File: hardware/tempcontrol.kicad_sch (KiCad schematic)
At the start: 11 parts, among them J10 FAN1, J12 FAN2, U15 EMC2305-x-AP

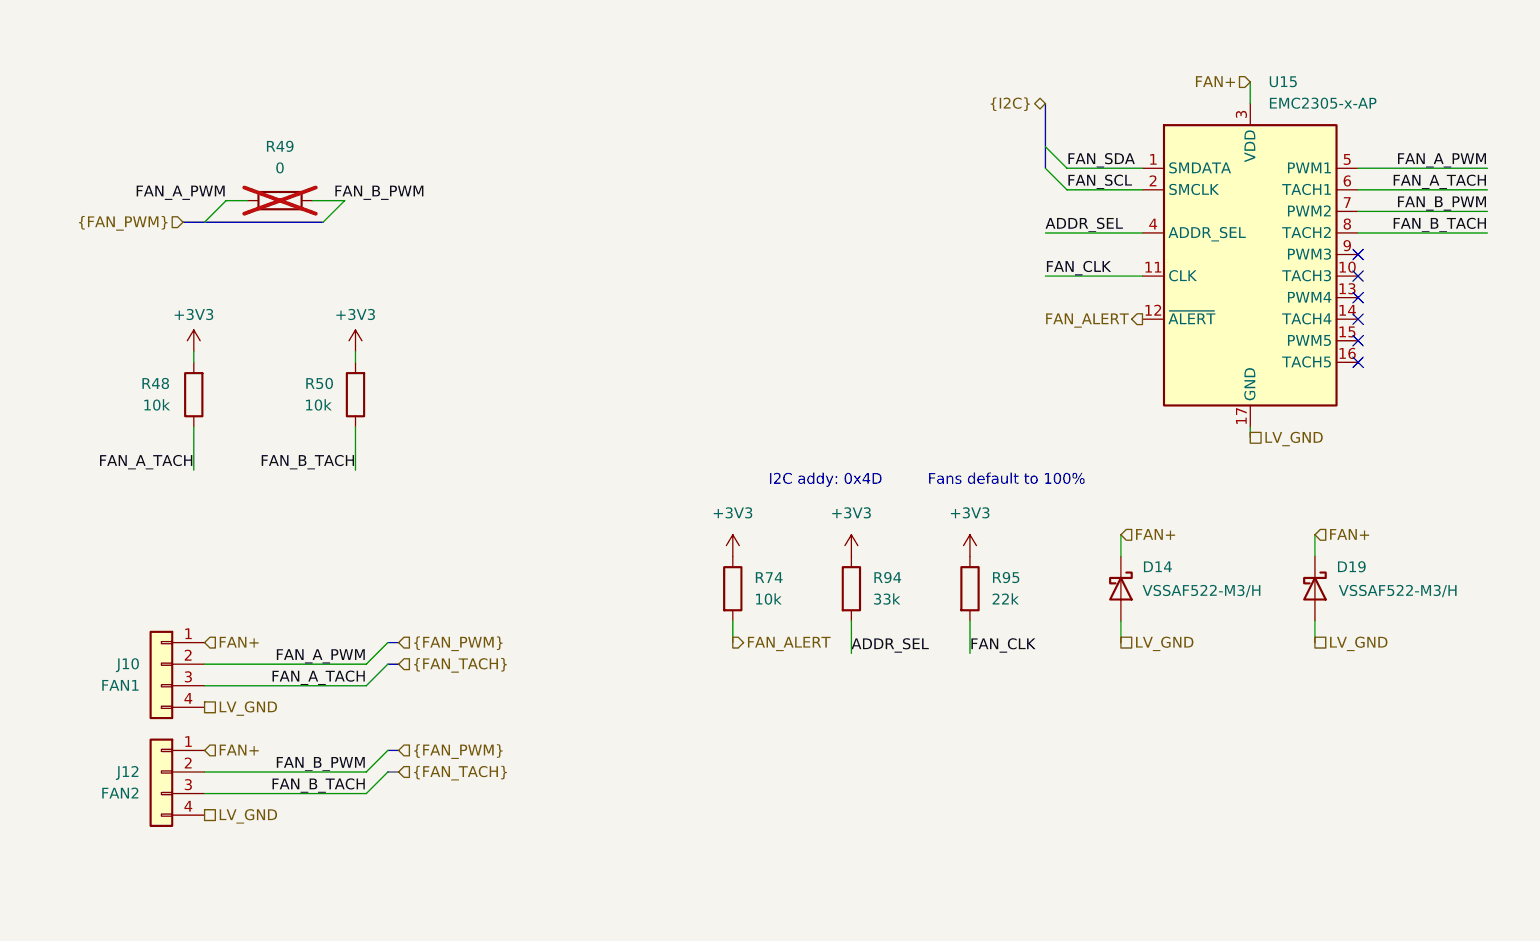
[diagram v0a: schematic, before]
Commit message: done all obbb specific reviews beside indicator led resistor values + math, goodnight
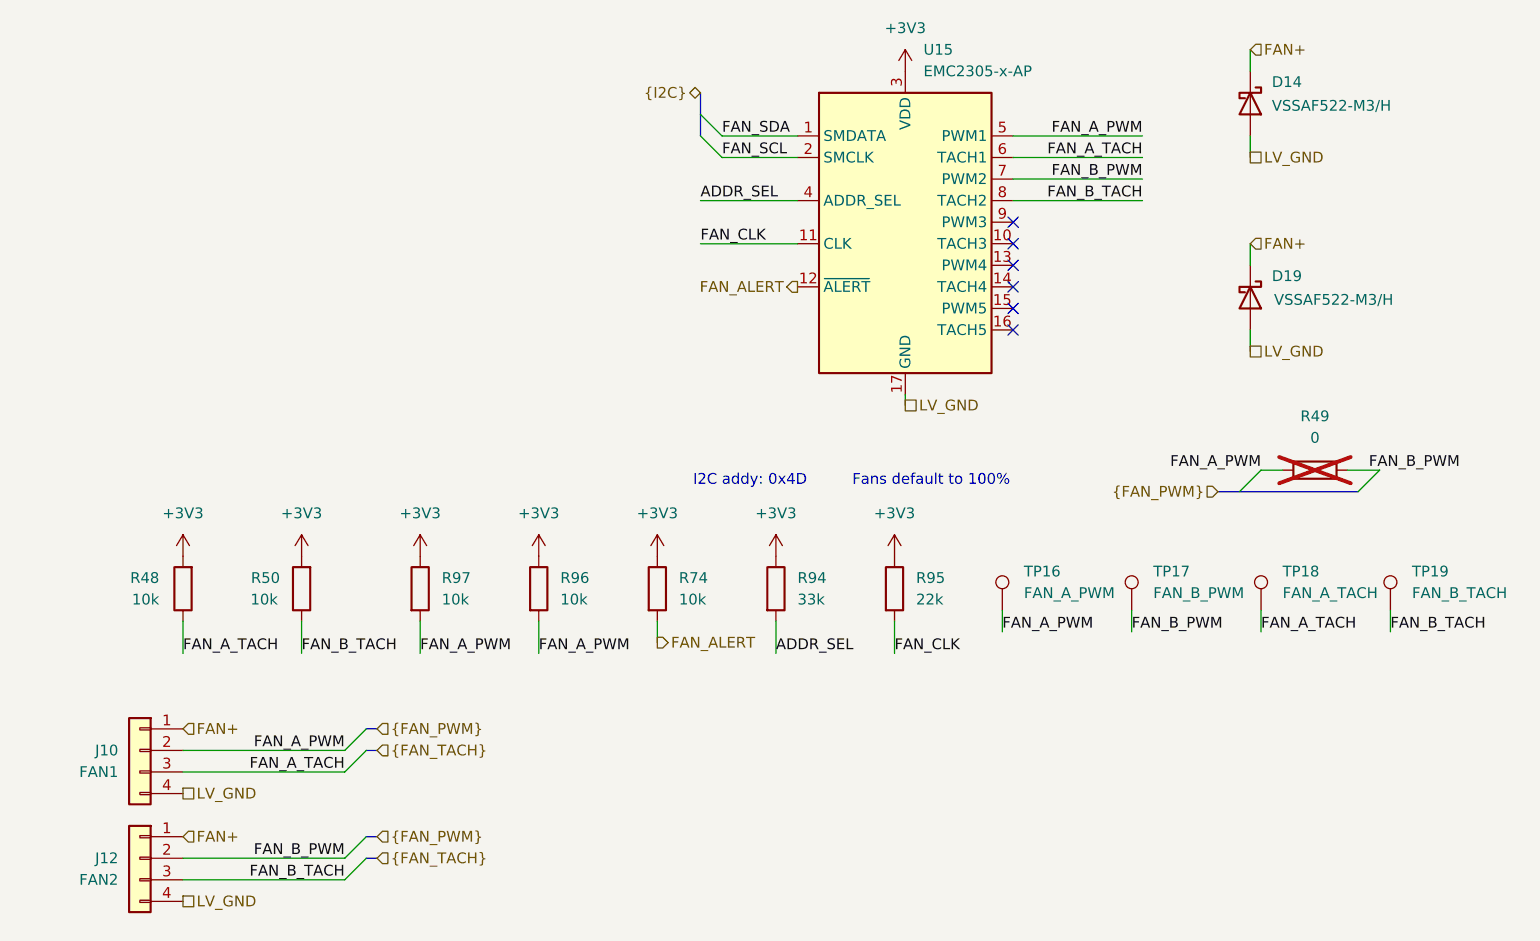
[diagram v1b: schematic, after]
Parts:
- added R96, R97: 10k, symbol Device:R
- added TP16: FAN_A_PWM, symbol Connector:TestPoint
- added TP17: FAN_B_PWM, symbol Connector:TestPoint
- added TP18: FAN_A_TACH, symbol Connector:TestPoint
- added TP19: FAN_B_TACH, symbol Connector:TestPoint
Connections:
- net +3V3: now also U15.3 (VDD), R96.1, R97.1
- net FAN+: no longer U15.3 (VDD)
- net FAN_A_PWM: now also R96.2, R97.2, TP16.1
- net FAN_A_TACH: now also TP18.1
- net FAN_B_PWM: now also TP17.1
- net FAN_B_TACH: now also TP19.1
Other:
- moved on the sheet: D14, D19, J10, J12, R48, R49, R50, R74, R94, R95, U15

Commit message: fixes only thing left is finish assigning footprints, its frozen
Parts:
- J10: renamed from J12; footprint (none) -> LHRS_Connectors:Molex_Nano-Fit_105309-xx04_1x04_P2.50mm_Vertical
- J9: renamed from J10; footprint (none) -> LHRS_Connectors:Molex_Nano-Fit_105309-xx04_1x04_P2.50mm_Vertical
- R88: renamed from R49; LCSC C21189 -> (none); LCSC P/N (none) -> C21189
- renumbered D14 to D20, D19 to D21, R48 to R81, R50 to R82, R97 to R83, R96 to R84, R74 to R85, R94 to R86, R95 to R87, TP16 to TP13, TP17 to TP14, TP18 to TP15, TP19 to TP16, U15 to U12
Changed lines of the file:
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@@
 		(dnp no)
 		(fields_autoplaced yes)
-		(property "Reference" "U15"
+		(property "Reference" "U12"
 			(at 126.6033 26.67 0)
 			(show_name no)
@@
 			(project "PS-LVCarrier"
 				(path "/9bab2d9d-20f3-40ef-8545-e1299efec47e/f9fba8b7-0cf3-4419-9ae4-4e9c55277e07"
-					(reference "U15")
+					(reference "U12")
 					(unit 1)
 				)
@@
 		(dnp no)
 		(fields_autoplaced yes)
-		(property "Reference" "R74"
+		(property "Reference" "R85"
 			(at 97.79 88.8999 0)
 			(show_name no)
@@
 			(project "PS-LVCarrier"
 				(path "/9bab2d9d-20f3-40ef-8545-e1299efec47e/f9fba8b7-0cf3-4419-9ae4-4e9c55277e07"
-					(reference "R74")
+					(reference "R85")
 					(unit 1)
 				)
@@
 		(in_pos_files yes)
 		(dnp no)
-		(property "Reference" "D19"
+		(property "Reference" "D21"
 			(at 167.64 53.34 90)
 			(show_name no)
@@
 			(project "PS-LVCarrier"
 				(path "/9bab2d9d-20f3-40ef-8545-e1299efec47e/f9fba8b7-0cf3-4419-9ae4-4e9c55277e07"
-					(reference "D19")
+					(reference "D21")
 					(unit 1)
 				)
@@
 		(dnp no)
 		(fields_autoplaced yes)
-		(property "Reference" "R96"
+		(property "Reference" "R84"
 			(at 83.82 88.8999 0)
 			(show_name no)
@@
 			(project "PS-LVCarrier"
 				(path "/9bab2d9d-20f3-40ef-8545-e1299efec47e/f9fba8b7-0cf3-4419-9ae4-4e9c55277e07"
-					(reference "R96")
+					(reference "R84")
 					(unit 1)
 				)
@@
 		(dnp no)
 		(fields_autoplaced yes)
-		(property "Reference" "TP19"
+		(property "Reference" "TP16"
 			(at 184.15 88.1379 0)
 			(show_name no)
@@
 			(project "PS-LVCarrier"
 				(path "/9bab2d9d-20f3-40ef-8545-e1299efec47e/f9fba8b7-0cf3-4419-9ae4-4e9c55277e07"
-					(reference "TP19")
+					(reference "TP16")
 					(unit 1)
 				)
@@
 		(dnp no)
 		(fields_autoplaced yes)
-		(property "Reference" "#PWR0172"
+		(property "Reference" "#PWR0104"
 			(at 124.46 33.02 0)
 			(hide yes)
@@
 			(project "PS-LVCarrier"
 				(path "/9bab2d9d-20f3-40ef-8545-e1299efec47e/f9fba8b7-0cf3-4419-9ae4-4e9c55277e07"
-					(reference "#PWR0172")
+					(reference "#PWR0104")
 					(unit 1)
 				)
@@
 		(dnp no)
 		(fields_autoplaced yes)
-		(property "Reference" "R97"
+		(property "Reference" "R83"
 			(at 69.85 88.8999 0)
 			(show_name no)
@@
 			(project "PS-LVCarrier"
 				(path "/9bab2d9d-20f3-40ef-8545-e1299efec47e/f9fba8b7-0cf3-4419-9ae4-4e9c55277e07"
-					(reference "R97")
+					(reference "R83")
 					(unit 1)
 				)
@@
 		(dnp no)
 		(fields_autoplaced yes)
-		(property "Reference" "#PWR0170"
+		(property "Reference" "#PWR097"
 			(at 39.37 90.17 0)
 			(hide yes)
@@
 			(project "PS-LVCarrier"
 				(path "/9bab2d9d-20f3-40ef-8545-e1299efec47e/f9fba8b7-0cf3-4419-9ae4-4e9c55277e07"
-					(reference "#PWR0170")
+					(reference "#PWR097")
 					(unit 1)
 				)
@@
 		(dnp no)
 		(fields_autoplaced yes)
-		(property "Reference" "TP18"
+		(property "Reference" "TP15"
 			(at 168.91 88.1379 0)
 			(show_name no)
@@
 			(project "PS-LVCarrier"
 				(path "/9bab2d9d-20f3-40ef-8545-e1299efec47e/f9fba8b7-0cf3-4419-9ae4-4e9c55277e07"
-					(reference "TP18")
+					(reference "TP15")
 					(unit 1)
 				)
@@
 		(in_pos_files yes)
 		(dnp no)
-		(property "Reference" "R50"
+		(property "Reference" "R82"
 			(at 50.8 88.9 0)
 			(show_name no)
@@
 			(project "PS-LVCarrier"
 				(path "/9bab2d9d-20f3-40ef-8545-e1299efec47e/f9fba8b7-0cf3-4419-9ae4-4e9c55277e07"
-					(reference "R50")
+					(reference "R82")
 					(unit 1)
 				)
@@
 		(dnp no)
 		(fields_autoplaced yes)
-		(property "Reference" "#PWR0168"
+		(property "Reference" "#PWR0100"
 			(at 81.28 90.17 0)
 			(hide yes)
@@
 			(project "PS-LVCarrier"
 				(path "/9bab2d9d-20f3-40ef-8545-e1299efec47e/f9fba8b7-0cf3-4419-9ae4-4e9c55277e07"
-					(reference "#PWR0168")
+					(reference "#PWR0100")
 					(unit 1)
 				)
@@
 		(dnp no)
 		(fields_autoplaced yes)
-		(property "Reference" "#PWR0165"
+		(property "Reference" "#PWR0101"
 			(at 95.25 90.17 0)
 			(hide yes)
@@
 			(project "PS-LVCarrier"
 				(path "/9bab2d9d-20f3-40ef-8545-e1299efec47e/f9fba8b7-0cf3-4419-9ae4-4e9c55277e07"
-					(reference "#PWR0165")
+					(reference "#PWR0101")
 					(unit 1)
 				)
@@
 		(dnp no)
 		(fields_autoplaced yes)
-		(property "Reference" "#PWR0169"
+		(property "Reference" "#PWR099"
 			(at 67.31 90.17 0)
 			(hide yes)
@@
 			(project "PS-LVCarrier"
 				(path "/9bab2d9d-20f3-40ef-8545-e1299efec47e/f9fba8b7-0cf3-4419-9ae4-4e9c55277e07"
-					(reference "#PWR0169")
+					(reference "#PWR099")
 					(unit 1)
 				)
@@
 		(dnp no)
 		(fields_autoplaced yes)
-		(property "Reference" "R94"
+		(property "Reference" "R86"
 			(at 111.76 88.8999 0)
 			(show_name no)
@@
 			(project "PS-LVCarrier"
 				(path "/9bab2d9d-20f3-40ef-8545-e1299efec47e/f9fba8b7-0cf3-4419-9ae4-4e9c55277e07"
-					(reference "R94")
+					(reference "R86")
 					(unit 1)
 				)
@@
 		(in_pos_files yes)
 		(dnp no)
-		(property "Reference" "J10"
+		(property "Reference" "J9"
 			(at 31.75 109.2199 0)
 			(show_name no)
@@
 			)
 		)
-		(property "Footprint" ""
+		(property "Footprint" "LHRS_Connectors:Molex_Nano-Fit_105309-xx04_1x04_P2.50mm_Vertical"
 			(at 34.29 109.22 0)
 			(hide yes)
@@
 			(project "PS-LVCarrier"
 				(path "/9bab2d9d-20f3-40ef-8545-e1299efec47e/f9fba8b7-0cf3-4419-9ae4-4e9c55277e07"
-					(reference "J10")
+					(reference "J9")
 					(unit 1)
 				)
@@
 		(in_pos_files yes)
 		(dnp no)
-		(property "Reference" "J12"
+		(property "Reference" "J10"
 			(at 31.75 121.9199 0)
 			(show_name no)
@@
 			)
 		)
-		(property "Footprint" ""
+		(property "Footprint" "LHRS_Connectors:Molex_Nano-Fit_105309-xx04_1x04_P2.50mm_Vertical"
 			(at 34.29 121.92 0)
 			(hide yes)
@@
 			(project "PS-LVCarrier"
 				(path "/9bab2d9d-20f3-40ef-8545-e1299efec47e/f9fba8b7-0cf3-4419-9ae4-4e9c55277e07"
-					(reference "J12")
+					(reference "J10")
 					(unit 1)
 				)
@@
 		(dnp no)
 		(fields_autoplaced yes)
-		(property "Reference" "TP17"
+		(property "Reference" "TP14"
 			(at 153.67 88.1379 0)
 			(show_name no)
@@
 			(project "PS-LVCarrier"
 				(path "/9bab2d9d-20f3-40ef-8545-e1299efec47e/f9fba8b7-0cf3-4419-9ae4-4e9c55277e07"
-					(reference "TP17")
+					(reference "TP14")
 					(unit 1)
 				)
@@
 		(dnp no)
 		(fields_autoplaced yes)
-		(property "Reference" "TP16"
+		(property "Reference" "TP13"
 			(at 138.43 88.1379 0)
 			(show_name no)
@@
 			(project "PS-LVCarrier"
 				(path "/9bab2d9d-20f3-40ef-8545-e1299efec47e/f9fba8b7-0cf3-4419-9ae4-4e9c55277e07"
-					(reference "TP16")
+					(reference "TP13")
 					(unit 1)
 				)
@@
 		(dnp no)
 		(fields_autoplaced yes)
-		(property "Reference" "#PWR0167"
+		(property "Reference" "#PWR0103"
 			(at 123.19 90.17 0)
 			(hide yes)
@@
 			(project "PS-LVCarrier"
 				(path "/9bab2d9d-20f3-40ef-8545-e1299efec47e/f9fba8b7-0cf3-4419-9ae4-4e9c55277e07"
-					(reference "#PWR0167")
+					(reference "#PWR0103")
 					(unit 1)
 				)
@@
 		(dnp no)
 		(fields_autoplaced yes)
-		(property "Reference" "R95"
+		(property "Reference" "R87"
 			(at 125.73 88.8999 0)
 			(show_name no)
@@
 			(project "PS-LVCarrier"
 				(path "/9bab2d9d-20f3-40ef-8545-e1299efec47e/f9fba8b7-0cf3-4419-9ae4-4e9c55277e07"
-					(reference "R95")
+					(reference "R87")
 					(unit 1)
 				)
@@
 		(in_pos_files yes)
 		(dnp no)
-		(property "Reference" "D14"
+		(property "Reference" "D20"
 			(at 167.64 30.48 90)
 			(show_name no)
@@
 			(project "PS-LVCarrier"
 				(path "/9bab2d9d-20f3-40ef-8545-e1299efec47e/f9fba8b7-0cf3-4419-9ae4-4e9c55277e07"
-					(reference "D14")
+					(reference "D20")
 					(unit 1)
 				)
@@
 		(dnp yes)
 		(fields_autoplaced yes)
-		(property "Reference" "R49"
+		(property "Reference" "R88"
 			(at 172.72 69.85 90)
 			(show_name no)
@@
 			)
 		)
-		(property "LCSC" "C21189"
+		(property "LCSC" ""
 			(at 172.72 76.2 90)
 			(hide yes)
@@
 			)
 		)
+		(property "LCSC P/N" "C21189"
+			(at 172.72 76.2 90)
+			(hide yes)
+			(show_name no)
+			(do_not_autoplace no)
+			(effects
+				(font
+					(size 1.27 1.27)
+				)
+			)
+		)
 		(pin "1"
 		)
@@
 			(project "PS-LVCarrier"
 				(path "/9bab2d9d-20f3-40ef-8545-e1299efec47e/f9fba8b7-0cf3-4419-9ae4-4e9c55277e07"
-					(reference "R49")
+					(reference "R88")
 					(unit 1)
 				)
@@
 		(in_pos_files yes)
 		(dnp no)
-		(property "Reference" "R48"
+		(property "Reference" "R81"
 			(at 36.576 88.9 0)
 			(show_name no)
@@
 			(project "PS-LVCarrier"
 				(path "/9bab2d9d-20f3-40ef-8545-e1299efec47e/f9fba8b7-0cf3-4419-9ae4-4e9c55277e07"
-					(reference "R48")
+					(reference "R81")
 					(unit 1)
 				)
@@
 		(dnp no)
 		(fields_autoplaced yes)
-		(property "Reference" "#PWR0171"
+		(property "Reference" "#PWR098"
 			(at 53.34 90.17 0)
 			(hide yes)
@@
 			(project "PS-LVCarrier"
 				(path "/9bab2d9d-20f3-40ef-8545-e1299efec47e/f9fba8b7-0cf3-4419-9ae4-4e9c55277e07"
-					(reference "#PWR0171")
+					(reference "#PWR098")
 					(unit 1)
 				)
@@
 		(dnp no)
 		(fields_autoplaced yes)
-		(property "Reference" "#PWR0166"
+		(property "Reference" "#PWR0102"
 			(at 109.22 90.17 0)
 			(hide yes)
@@
 			(project "PS-LVCarrier"
 				(path "/9bab2d9d-20f3-40ef-8545-e1299efec47e/f9fba8b7-0cf3-4419-9ae4-4e9c55277e07"
-					(reference "#PWR0166")
-					(unit 1)
-				)
+					(reference "#PWR0102")
+					(unit 1)
+				)

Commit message: switching branches
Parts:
- R81, R82: LCSC P/N (none) -> C25804
- R83, R84, R85: footprint (none) -> Resistor_SMD:R_0603_1608Metric_Pad0.98x0.95mm_HandSolder; LCSC P/N (none) -> C25804
- R86: footprint (none) -> Resistor_SMD:R_0603_1608Metric_Pad0.98x0.95mm_HandSolder; LCSC P/N (none) -> C177291
- R87: footprint (none) -> Resistor_SMD:R_0603_1608Metric_Pad0.98x0.95mm_HandSolder; LCSC P/N (none) -> C31850
- TP13, TP14, TP15, TP16: footprint (none) -> TestPoint:TestPoint_THTPad_D3.0mm_Drill1.5mm
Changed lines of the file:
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@@
 			)
 		)
-		(property "Footprint" ""
+		(property "Footprint" "Resistor_SMD:R_0603_1608Metric_Pad0.98x0.95mm_HandSolder"
 			(at 93.472 90.17 90)
 			(hide yes)
@@
 		)
 		(property "Description" "Resistor"
+			(at 95.25 90.17 0)
+			(hide yes)
+			(show_name no)
+			(do_not_autoplace no)
+			(effects
+				(font
+					(size 1.27 1.27)
+				)
+			)
+		)
+		(property "LCSC P/N" "C25804"
 			(at 95.25 90.17 0)
 			(hide yes)
@@
 			)
 		)
-		(property "Footprint" ""
+		(property "Footprint" "Resistor_SMD:R_0603_1608Metric_Pad0.98x0.95mm_HandSolder"
 			(at 79.502 90.17 90)
 			(hide yes)
@@
 		)
 		(property "Description" "Resistor"
+			(at 81.28 90.17 0)
+			(hide yes)
+			(show_name no)
+			(do_not_autoplace no)
+			(effects
+				(font
+					(size 1.27 1.27)
+				)
+			)
+		)
+		(property "LCSC P/N" "C25804"
 			(at 81.28 90.17 0)
 			(hide yes)
@@
 			)
 		)
-		(property "Footprint" ""
+		(property "Footprint" "TestPoint:TestPoint_THTPad_D3.0mm_Drill1.5mm"
 			(at 186.69 92.71 0)
 			(hide yes)
@@
 			)
 		)
-		(property "Footprint" ""
+		(property "Footprint" "Resistor_SMD:R_0603_1608Metric_Pad0.98x0.95mm_HandSolder"
 			(at 65.532 90.17 90)
 			(hide yes)
@@
 		)
 		(property "Description" "Resistor"
+			(at 67.31 90.17 0)
+			(hide yes)
+			(show_name no)
+			(do_not_autoplace no)
+			(effects
+				(font
+					(size 1.27 1.27)
+				)
+			)
+		)
+		(property "LCSC P/N" "C25804"
 			(at 67.31 90.17 0)
 			(hide yes)
@@
 			)
 		)
-		(property "Footprint" ""
+		(property "Footprint" "TestPoint:TestPoint_THTPad_D3.0mm_Drill1.5mm"
 			(at 171.45 92.71 0)
 			(hide yes)
@@
 		(property "LCSC" "C25804"
 			(at 53.34 90.17 90)
+			(hide yes)
+			(show_name no)
+			(do_not_autoplace no)
+			(effects
+				(font
+					(size 1.27 1.27)
+				)
+			)
+		)
+		(property "LCSC P/N" "C25804"
+			(at 53.34 90.17 0)
 			(hide yes)
 			(show_name no)
@@
 			)
 		)
-		(property "Footprint" ""
+		(property "Footprint" "Resistor_SMD:R_0603_1608Metric_Pad0.98x0.95mm_HandSolder"
 			(at 107.442 90.17 90)
 			(hide yes)
@@
 		)
 		(property "Description" "Resistor"
+			(at 109.22 90.17 0)
+			(hide yes)
+			(show_name no)
+			(do_not_autoplace no)
+			(effects
+				(font
+					(size 1.27 1.27)
+				)
+			)
+		)
+		(property "LCSC P/N" "C177291"
 			(at 109.22 90.17 0)
 			(hide yes)
@@
 			)
 		)
-		(property "Footprint" ""
+		(property "Footprint" "TestPoint:TestPoint_THTPad_D3.0mm_Drill1.5mm"
 			(at 156.21 92.71 0)
 			(hide yes)
@@
 			)
 		)
-		(property "Footprint" ""
+		(property "Footprint" "TestPoint:TestPoint_THTPad_D3.0mm_Drill1.5mm"
 			(at 140.97 92.71 0)
 			(hide yes)
@@
 			)
 		)
-		(property "Footprint" ""
+		(property "Footprint" "Resistor_SMD:R_0603_1608Metric_Pad0.98x0.95mm_HandSolder"
 			(at 121.412 90.17 90)
 			(hide yes)
@@
 		)
 		(property "Description" "Resistor"
+			(at 123.19 90.17 0)
+			(hide yes)
+			(show_name no)
+			(do_not_autoplace no)
+			(effects
+				(font
+					(size 1.27 1.27)
+				)
+			)
+		)
+		(property "LCSC P/N" "C31850"
 			(at 123.19 90.17 0)
 			(hide yes)
@@
 			(hide yes)
 			(show_name no)
+			(do_not_autoplace no)
+			(effects
+				(font
+					(size 1.27 1.27)
+				)
+			)
+		)
+		(property "LCSC P/N" "C25804"
+			(at 39.37 90.17 0)
+			(hide yes)
+			(show_name no)
